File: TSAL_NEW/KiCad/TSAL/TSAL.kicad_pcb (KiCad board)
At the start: 2 copper layers, 74.8 x 40.6 mm, 39 parts, among them J1 HV INPUT, J2 HV GND, J3 Conn_01x03, J4 Conn_01x04, J5 Conn_01x02, Q1 BSS84, Q2 BSS84, U1 LTV-817S, U2 LR8K4-G, U4 LM555

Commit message: small updates
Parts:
- added G***: LOGO, aero_footprint:AERO_Logo_15x6mm, B.Cu at (164.2, 122.8)
- J3: footprint Connector_JST:JST_PH_B3B-PH-K_1x03_P2.00mm_Vertical -> Connector_PinHeader_2.54mm:PinHeader_1x03_P2.54mm_Vertical
- moved J3 0.61 mm to (156.8, 101.7), turned to 180 degrees

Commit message: 3d updates
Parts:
- added REF**: JUMPER_BLUE, AERO-footprints:JUMPER_BLUE, F.Cu at (156.7, 96.5)
- F1: footprint Fuse:Fuse_1812_4532Metric_Pad1.30x3.40mm_HandSolder -> AERO-footprints:Fuse_1812_4532Metric_Pad1.30x3.40mm_HandSolder
- J1, J2: footprint Connector_TE-Connectivity:TE_MATE-N-LOK_1-770866-x_1x02_P4.14mm_Vertical -> AERO-footprints:TE_MATE-N-LOK_1-770866-x_1x02_P4.14mm_Vertical

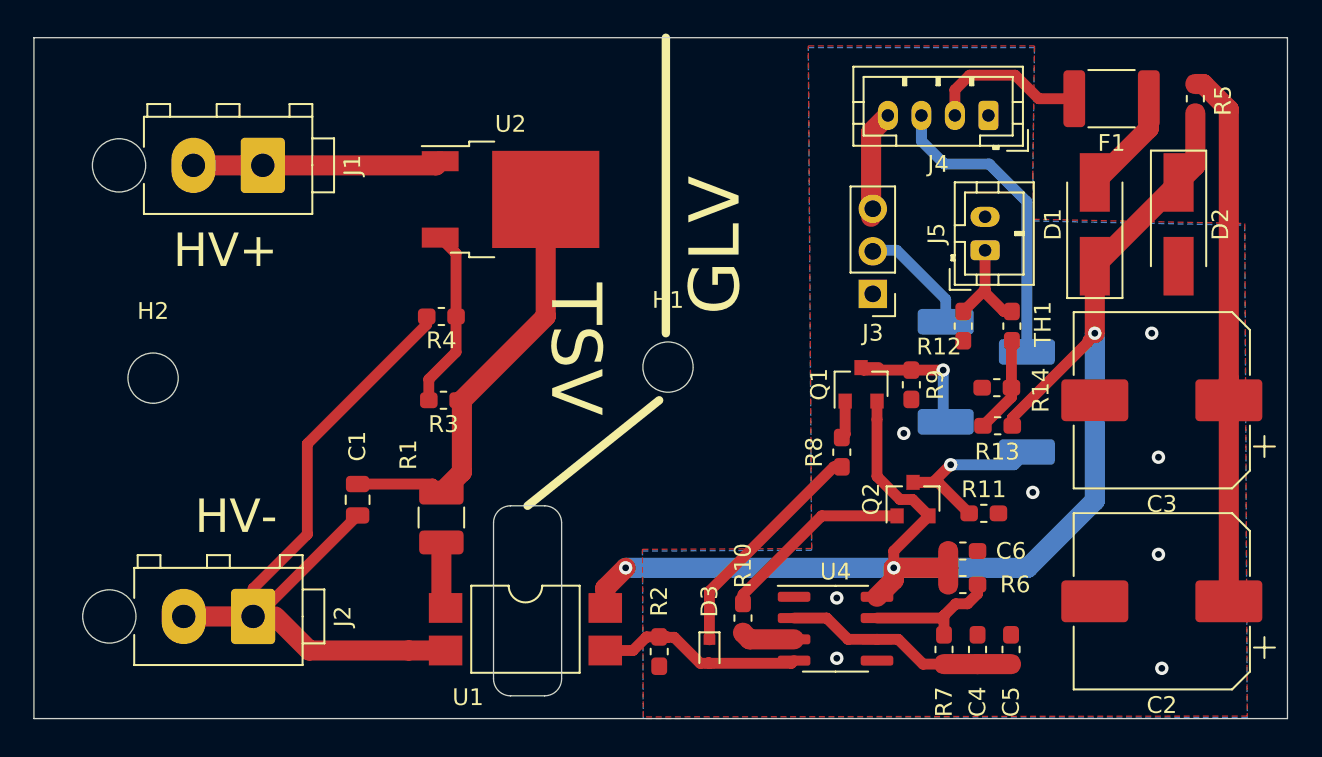
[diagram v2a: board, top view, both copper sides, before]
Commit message: Changed HVInput to Optoisolator and added HV sense pin
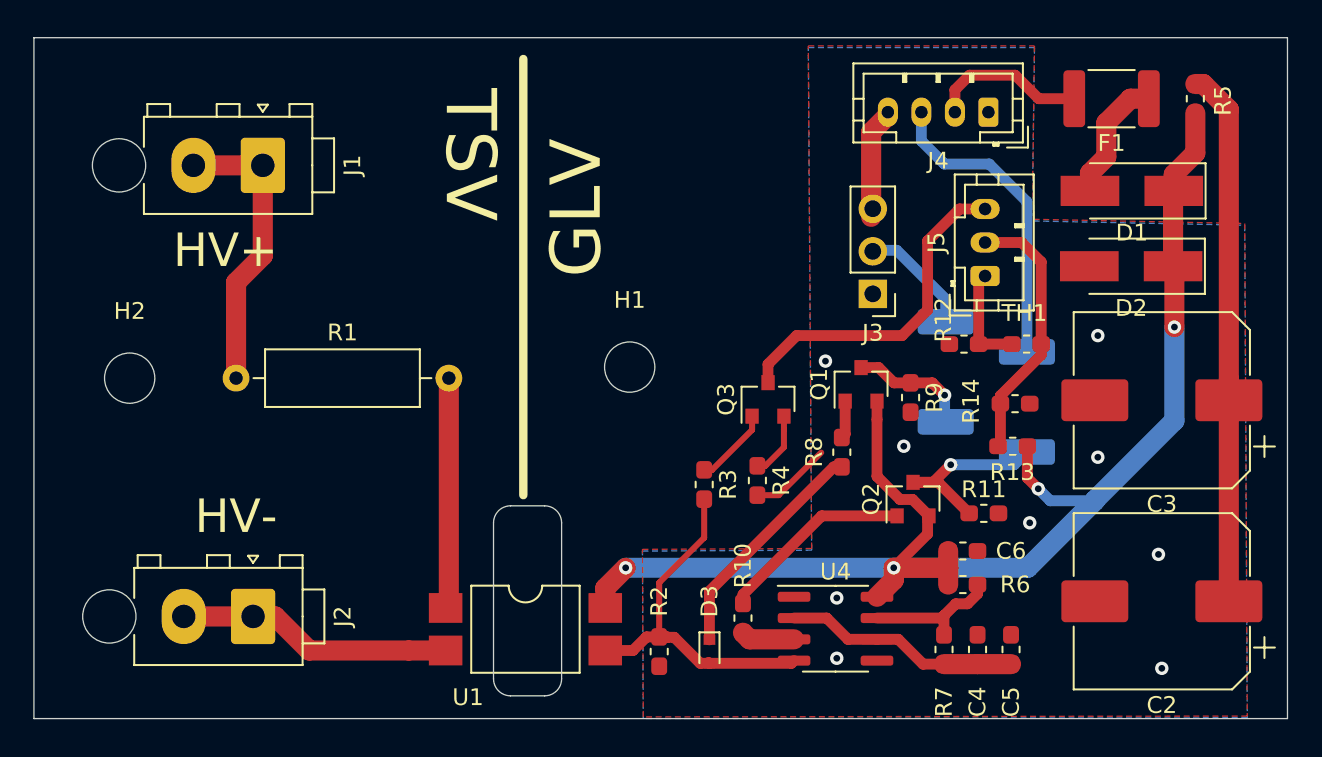
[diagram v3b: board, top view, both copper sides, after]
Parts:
- removed C1: C2012X7S2A105K125AB, Capacitor_SMD:C_0805_2012Metric
- removed G***: LOGO, aero_footprint:AERO_Logo_15x6mm
- removed REF**: JUMPER_BLUE, AERO-footprints:JUMPER_BLUE
- removed U2: LR8K4-G, Package_TO_SOT_SMD:TO-252-2
- added Q3: 2N7002, Package_TO_SOT_SMD:SOT-23, F.Cu at (150.5, 108.0)
- F1: footprint AERO-footprints:Fuse_1812_4532Metric_Pad1.30x3.40mm_HandSolder -> Fuse:Fuse_1812_4532Metric_Pad1.30x3.40mm_HandSolder
- J1, J2: footprint AERO-footprints:TE_MATE-N-LOK_1-770866-x_1x02_P4.14mm_Vertical -> Connector_TE-Connectivity:TE_MATE-N-LOK_1-770866-x_1x02_P4.14mm_Vertical
- J4: value Conn_01x04 -> B4B-PH-K
- J5: footprint Connector_JST:JST_PH_B2B-PH-K_1x02_P2.00mm_Vertical -> Connector_JST:JST_PH_B3B-PH-K_1x03_P2.00mm_Vertical
- R1: value 549 -> 33k axial; footprint Resistor_SMD:R_1210_3225Metric_Pad1.42x2.65mm_HandSolder -> Resistor_THT:R_Axial_DIN0309_L9.0mm_D3.2mm_P12.70mm_Horizontal
- R3: value 180k -> 100
- R4: value 20k -> 10k
- TH1: value Thermistor -> NCU18XH103F60RB
- moved R4 21.2 mm to (149.9, 112.8), turned to 270 degrees
- moved R3 16.4 mm to (146.7, 113.0), turned to 270 degrees
- moved R1 14.8 mm to (118.7, 106.7), turned to 0 degrees
- moved D2 3.77 mm to (172.2, 100.0), turned to 180 degrees
- moved D1 2.98 mm to (172.2, 95.5), turned to 180 degrees
- moved H1 2.29 mm to (142.2, 106.0)
- moved J5 1.53 mm to (163.4, 100.6)
- moved R13 1.52 mm to (165.1, 110.7)
- moved R14 1.45 mm to (165.2, 108.2), turned to 0 degrees
- moved H2 1.40 mm to (112.4, 106.7)
- moved TH1 1.38 mm to (165.9, 104.6), turned to 0 degrees
- moved R12 1.07 mm to (162.2, 104.6), turned to 0 degrees
- moved R9 0.76 mm to (159.0, 107.8)
- moved J4 0.19 mm to (163.7, 90.8)
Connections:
- J5 pad 2: GND -> Net-(J5-Pad2)
- R1 pad 1: +12VA -> /HV+
- R13 pad 2: Net-(R13-Pad2) -> Net-(J5-Pad2)
- R14 pad 1: Net-(R13-Pad2) -> Net-(J5-Pad2)
- R3 pad 1: +12VA -> Net-(Q3-Pad1)
- R3 pad 2: Net-(R3-Pad2) -> /HV_PRES
- R4 pad 1: Net-(R3-Pad2) -> Net-(Q3-Pad2)
- R4 pad 2: GNDA -> GND
- TH1 pad 2: Net-(R13-Pad2) -> Net-(J5-Pad2)
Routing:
- net GNDA: track 47.4 -> 16.5 mm
- net +12VA: track 25.3 -> 0.00 mm
- net /HV_PRES_TRUE: track 0.00 -> 20.3 mm
- net Net-(J5-Pad2): track 0.00 -> 15.9 mm
- net Net-(R3-Pad2): track 10.8 -> 0.00 mm
- net Net-(R1-Pad2): track 4.01 -> 13.8 mm
- net /HV_PRES: track 12.4 -> 21.7 mm
- net Net-(R13-Pad2): track 5.79 -> 0.00 mm
- net GND: track 0.00 -> 4.86 mm, vias 8 -> 9
- net Net-(Q3-Pad1): track 0.00 -> 4.67 mm
- net Net-(Q3-Pad2): track 0.00 -> 3.90 mm
- net /HV+: track 14.8 -> 17.5 mm
- net Net-(Q1-Pad3): track 9.16 -> 7.29 mm
- net Net-(D1-Pad2): track 6.34 -> 8.15 mm
- net +12V: track 85.7 -> 84.6 mm, vias 3 -> 4
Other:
- board text added: "TSAL rev2 G.Spearing 20.0225"
- board text removed: "TSAL G.Spearing 20.0131"

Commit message: change resistor
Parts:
- R1: footprint Resistor_THT:R_Axial_DIN0309_L9.0mm_D3.2mm_P12.70mm_Horizontal -> Resistor_THT:R_Axial_DIN0309_L9.0mm_D3.2mm_P20.32mm_Horizontal
- moved R1 16.0 mm to (128.5, 94.0), turned to 270 degrees
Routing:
- net Net-(R1-Pad2): track 13.8 -> 8.12 mm
- net /HV+: track 17.5 -> 12.3 mm
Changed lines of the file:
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@@
     (thickness 1.6)
     (drawings 27)
-    (tracks 164)
+    (tracks 163)
     (zones 0)
     (modules 38)
@@
   )
   (setup
-    (last_trace_width 0.65)
+    (last_trace_width 1.2)
     (user_trace_width 0.24)
     (user_trace_width 0.36)
@@
     (add_net GNDA)
   )
+  (module Resistor_THT:R_Axial_DIN0309_L9.0mm_D3.2mm_P20.32mm_Horizontal (layer F.Cu)
+    (at 128.524 93.98 270)
+    (descr "Resistor, Axial_DIN0309 series, Axial, Horizontal, pin pitch=20.32mm, 0.5W = 1/2W, length*diameter=9*3.2mm^2, http://cdn-reichelt.de/documents/datenblatt/B400/1_4W%23YAG.pdf")
+    (tags "Resistor Axial_DIN0309 series Axial Horizontal pin pitch 20.32mm 0.5W = 1/2W length 9mm diameter 3.2mm")
+    (fp_text reference R1 (at 10.16 -2.72 90) (layer F.SilkS)
+      (effects (font (size 1 1) (thickness 0.15)))
+    )
+    (fp_text value "33k axial" (at 10.16 2.72 90) (layer F.Fab)
+      (effects (font (size 1 1) (thickness 0.15)))
+    )
+    (fp_text user %R (at 10.16 0 90) (layer F.Fab)
+      (effects (font (size 1 1) (thickness 0.15)))
+    )
+    (fp_line (start 21.37 -1.85) (end -1.05 -1.85) (layer F.CrtYd) (width 0.05))
+    (fp_line (start 21.37 1.85) (end 21.37 -1.85) (layer F.CrtYd) (width 0.05))
+    (fp_line (start -1.05 1.85) (end 21.37 1.85) (layer F.CrtYd) (width 0.05))
+    (fp_line (start -1.05 -1.85) (end -1.05 1.85) (layer F.CrtYd) (width 0.05))
+    (fp_line (start 19.28 0) (end 14.78 0) (layer F.SilkS) (width 0.12))
+    (fp_line (start 1.04 0) (end 5.54 0) (layer F.SilkS) (width 0.12))
+    (fp_line (start 14.78 -1.72) (end 5.54 -1.72) (layer F.SilkS) (width 0.12))
+    (fp_line (start 14.78 1.72) (end 14.78 -1.72) (layer F.SilkS) (width 0.12))
+    (fp_line (start 5.54 1.72) (end 14.78 1.72) (layer F.SilkS) (width 0.12))
+    (fp_line (start 5.54 -1.72) (end 5.54 1.72) (layer F.SilkS) (width 0.12))
+    (fp_line (start 20.32 0) (end 14.66 0) (layer F.Fab) (width 0.1))
+    (fp_line (start 0 0) (end 5.66 0) (layer F.Fab) (width 0.1))
+    (fp_line (start 14.66 -1.6) (end 5.66 -1.6) (layer F.Fab) (width 0.1))
+    (fp_line (start 14.66 1.6) (end 14.66 -1.6) (layer F.Fab) (width 0.1))
+    (fp_line (start 5.66 1.6) (end 14.66 1.6) (layer F.Fab) (width 0.1))
+    (fp_line (start 5.66 -1.6) (end 5.66 1.6) (layer F.Fab) (width 0.1))
+    (pad 2 thru_hole oval (at 20.32 0 270) (size 1.6 1.6) (drill 0.8) (layers *.Cu *.Mask)
+      (net 17 "Net-(R1-Pad2)"))
+    (pad 1 thru_hole circle (at 0 0 270) (size 1.6 1.6) (drill 0.8) (layers *.Cu *.Mask)
+      (net 3 /HV+))
+    (model ${KISYS3DMOD}/Resistor_THT.3dshapes/R_Axial_DIN0309_L9.0mm_D3.2mm_P20.32mm_Horizontal.wrl
+      (at (xyz 0 0 0))
+      (scale (xyz 1 1 1))
+      (rotate (xyz 0 0 0))
+    )
+  )
   (module Resistor_SMD:R_0603_1608Metric_Pad1.05x0.95mm_HandSolder (layer F.Cu)
     (at 149.86 112.79 270)
@@
       (net 22 "Net-(J5-Pad2)"))
     (model ${KISYS3DMOD}/Resistor_SMD.3dshapes/R_0603_1608Metric.wrl
-      (at (xyz 0 0 0))
-      (scale (xyz 1 1 1))
-      (rotate (xyz 0 0 0))
-    )
-  )
-  (module Resistor_THT:R_Axial_DIN0309_L9.0mm_D3.2mm_P12.70mm_Horizontal (layer F.Cu)
-    (at 118.745 106.68)
-    (descr "Resistor, Axial_DIN0309 series, Axial, Horizontal, pin pitch=12.7mm, 0.5W = 1/2W, length*diameter=9*3.2mm^2, http://cdn-reichelt.de/documents/datenblatt/B400/1_4W%23YAG.pdf")
-    (tags "Resistor Axial_DIN0309 series Axial Horizontal pin pitch 12.7mm 0.5W = 1/2W length 9mm diameter 3.2mm")
-    (fp_text reference R1 (at 6.35 -2.72) (layer F.SilkS)
-      (effects (font (size 1 1) (thickness 0.15)))
-    )
-    (fp_text value "33k axial" (at 6.35 2.72) (layer F.Fab)
-      (effects (font (size 1 1) (thickness 0.15)))
-    )
-    (fp_text user %R (at 6.35 0) (layer F.Fab)
-      (effects (font (size 1 1) (thickness 0.15)))
-    )
-    (fp_line (start 13.75 -1.85) (end -1.05 -1.85) (layer F.CrtYd) (width 0.05))
-    (fp_line (start 13.75 1.85) (end 13.75 -1.85) (layer F.CrtYd) (width 0.05))
-    (fp_line (start -1.05 1.85) (end 13.75 1.85) (layer F.CrtYd) (width 0.05))
-    (fp_line (start -1.05 -1.85) (end -1.05 1.85) (layer F.CrtYd) (width 0.05))
-    (fp_line (start 11.66 0) (end 10.97 0) (layer F.SilkS) (width 0.12))
-    (fp_line (start 1.04 0) (end 1.73 0) (layer F.SilkS) (width 0.12))
-    (fp_line (start 10.97 -1.72) (end 1.73 -1.72) (layer F.SilkS) (width 0.12))
-    (fp_line (start 10.97 1.72) (end 10.97 -1.72) (layer F.SilkS) (width 0.12))
-    (fp_line (start 1.73 1.72) (end 10.97 1.72) (layer F.SilkS) (width 0.12))
-    (fp_line (start 1.73 -1.72) (end 1.73 1.72) (layer F.SilkS) (width 0.12))
-    (fp_line (start 12.7 0) (end 10.85 0) (layer F.Fab) (width 0.1))
-    (fp_line (start 0 0) (end 1.85 0) (layer F.Fab) (width 0.1))
-    (fp_line (start 10.85 -1.6) (end 1.85 -1.6) (layer F.Fab) (width 0.1))
-    (fp_line (start 10.85 1.6) (end 10.85 -1.6) (layer F.Fab) (width 0.1))
-    (fp_line (start 1.85 1.6) (end 10.85 1.6) (layer F.Fab) (width 0.1))
-    (fp_line (start 1.85 -1.6) (end 1.85 1.6) (layer F.Fab) (width 0.1))
-    (pad 2 thru_hole oval (at 12.7 0) (size 1.6 1.6) (drill 0.8) (layers *.Cu *.Mask)
-      (net 17 "Net-(R1-Pad2)"))
-    (pad 1 thru_hole circle (at 0 0) (size 1.6 1.6) (drill 0.8) (layers *.Cu *.Mask)
-      (net 3 /HV+))
-    (model ${KISYS3DMOD}/Resistor_THT.3dshapes/R_Axial_DIN0309_L9.0mm_D3.2mm_P12.70mm_Horizontal.wrl
       (at (xyz 0 0 0))
       (scale (xyz 1 1 1))
@@
   (segment (start 158.27 122.27) (end 159.75 123.75) (width 0.65) (layer F.Cu) (net 2))
   (segment (start 116.2 93.98) (end 120.34 93.98) (width 1.2) (layer F.Cu) (net 3))
-  (segment (start 120.34 93.98) (end 120.34 99.37) (width 1.2) (layer F.Cu) (net 3))
-  (segment (start 118.745 100.965) (end 118.745 106.68) (width 1.2) (layer F.Cu) (net 3))
-  (segment (start 120.34 99.37) (end 118.745 100.965) (width 1.2) (layer F.Cu) (net 3))
+  (segment (start 120.34 93.98) (end 128.524 93.98) (width 1.2) (layer F.Cu) (net 3))
   (segment (start 129.052 122.936) (end 131.252 122.936) (width 1.2) (layer F.Cu) (net 4))
   (segment (start 123.113 122.936) (end 129.052 122.936) (width 1.2) (layer F.Cu) (net 4))
@@
   (segment (start 153.7 114.9) (end 149 119.6) (width 0.65) (layer F.Cu) (net 16))
   (segment (start 158.2 114.9) (end 153.7 114.9) (width 0.65) (layer F.Cu) (net 16))
-  (segment (start 131.445 120.203) (end 131.252 120.396) (width 1.2) (layer F.Cu) (net 17))
-  (segment (start 131.445 106.68) (end 131.445 120.203) (width 1.2) (layer F.Cu) (net 17))
+  (segment (start 128.524 114.3) (end 130.048 114.3) (width 1.2) (layer F.Cu) (net 17))
+  (segment (start 131.252 115.504) (end 131.252 120.396) (width 1.2) (layer F.Cu) (net 17))
+  (segment (start 130.048 114.3) (end 131.252 115.504) (width 1.2) (layer F.Cu) (net 17))
   (segment (start 161.1 101.975) (end 158.175 99.05) (width 0.65) (layer B.Cu) (net 18))
   (segment (start 158.175 99.05) (end 156.65 99.05) (width 0.65) (layer B.Cu) (net 18))

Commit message: Updated PCB Layout
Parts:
- added Ref**: Val**, AERO_BOARD:hv_small, B.Cu at (120.4, 108.2)
- added Ref**: Val**, AERO_BOARD:hv_small, F.Cu at (120.4, 108.2)
- R1: footprint Resistor_THT:R_Axial_DIN0309_L9.0mm_D3.2mm_P20.32mm_Horizontal -> Resistor_THT:R_Axial_DIN0516_L15.5mm_D5.0mm_P25.40mm_Horizontal
- moved R1 3.21 mm to (129.5, 90.9)
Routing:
- net Net-(R1-Pad2): track 8.12 -> 4.77 mm
- net /HV+: track 12.3 -> 14.6 mm

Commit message: Minor Layout Changes
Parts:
- removed D3: 1N4148WT, Diode_SMD:D_SOD-523
- removed R12: 10k, Resistor_SMD:R_0603_1608Metric_Pad1.05x0.95mm_HandSolder
- removed R13, R14: R, Resistor_SMD:R_0603_1608Metric_Pad1.05x0.95mm_HandSolder
- removed Ref** (x2): Val**, AERO_BOARD:hv_small
- J1, J2: footprint Connector_TE-Connectivity:TE_MATE-N-LOK_1-770866-x_1x02_P4.14mm_Vertical -> AERO_FOOT:TE_MATE-N-LOK_1-770866-x_1x02_P4.14mm_Vertical
- J3: value Conn_01x03 -> B3B-PH-K
- R1: value 33k axial -> ROX3SJ39K
- R4: value 10k -> 100
- moved D1 2.50 mm to (174.7, 95.5)
- moved R5 2.31 mm to (178.3, 89.9)
- moved R1 0.51 mm to (129.5, 91.4)
- moved F1 0.31 mm to (170.7, 90.0)
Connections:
- R8 pad 2: Net-(D3-Pad1) -> /HV_PRES
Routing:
- net /HV_PRES: track 21.7 -> 37.2 mm
- net Net-(D3-Pad1): track 13.9 -> 0.00 mm
- net Net-(J5-Pad2): track 15.9 -> 8.73 mm
- net +12V: track 84.6 -> 80.2 mm, vias 4 -> 3
- net Net-(D1-Pad2): track 8.15 -> 5.79 mm
- net /12V_CAP: track 32.0 -> 32.6 mm
